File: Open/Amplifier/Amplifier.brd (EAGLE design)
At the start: 20 x 13 mm, 14 parts

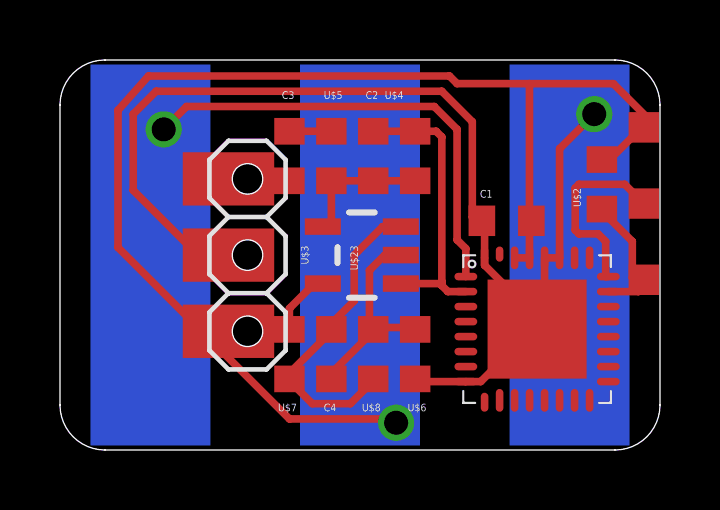
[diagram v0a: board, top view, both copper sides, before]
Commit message: Update Pinheader
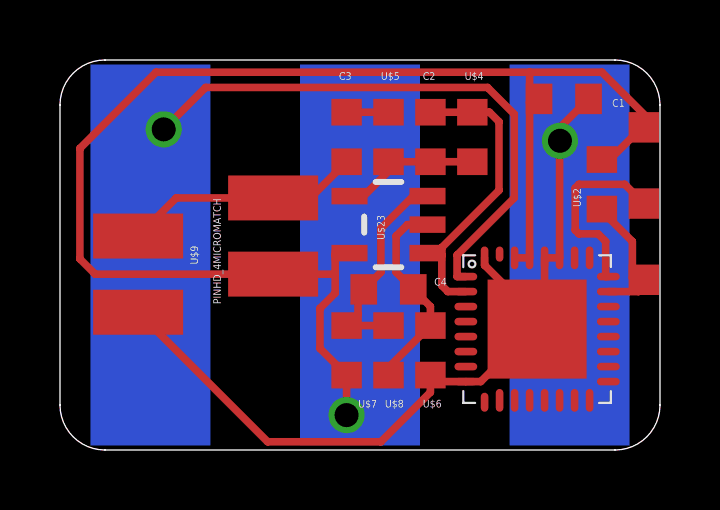
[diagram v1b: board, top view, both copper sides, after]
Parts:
- removed U$3: PINHD_32.54MOD, thar:PINHD_3_MOD
- added U$9: PINHD_4MICROMATCH, thar:MICROMATCH4P0L
- moved C1 4.49 mm to (18.5, 13.0), turned to 0 degrees
- moved C4 2.88 mm to (12.7, 6.60), turned to 180 degrees
- moved C3 2.01 mm to (11.3, 11.7)
- moved C2 2.01 mm to (14.1, 11.7)
- moved U$4 2.01 mm to (15.5, 11.7)
- moved U$5 2.01 mm to (12.7, 11.7)
- moved U$7 1.91 mm to (11.3, 4.57), turned to 90 degrees
- moved U$23 1.35 mm to (12.7, 8.76)
- moved U$6 0.52 mm to (14.1, 4.57)
- moved U$8 0.52 mm to (12.7, 4.57), turned to 90 degrees
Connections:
- net GND: now also U$9.P$1; no longer U$3.P$2
- net N$56: now also U$9.P$3, U$9.P$4; no longer U$3.P$1
- net VCC: now also U$9.P$2; no longer U$3.P$3
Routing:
- net GND: track 53.5 -> 41.0 mm
- net N$56: track 2.23 -> 7.97 mm
- net N$12: track 20.1 -> 23.8 mm
- net N$57: track 10.5 -> 7.11 mm
- net VCC: track 59.0 -> 59.9 mm
